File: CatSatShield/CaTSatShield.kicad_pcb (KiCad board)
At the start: 2 copper layers, 67.6 x 25 mm, 18 parts, among them J1 , J2 , J3 BME280, J4 CCS811

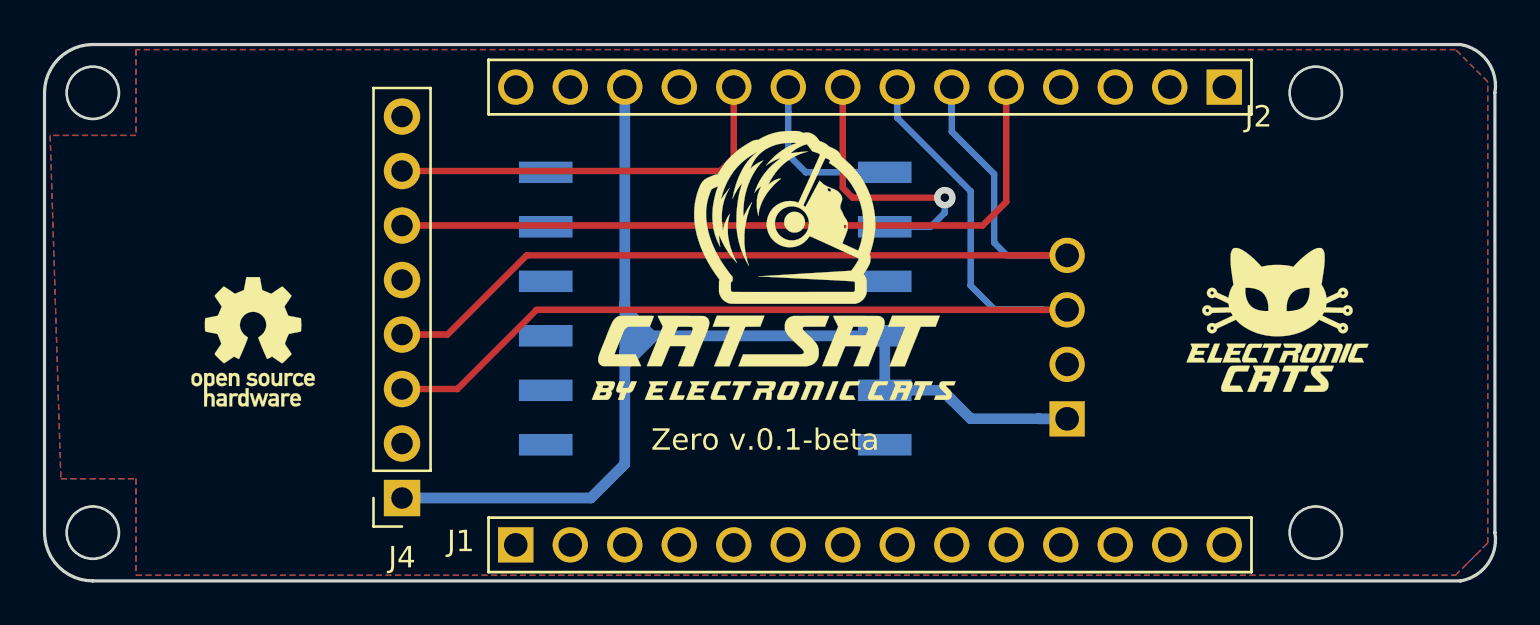
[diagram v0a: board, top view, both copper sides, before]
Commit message: connected pin wakeA6
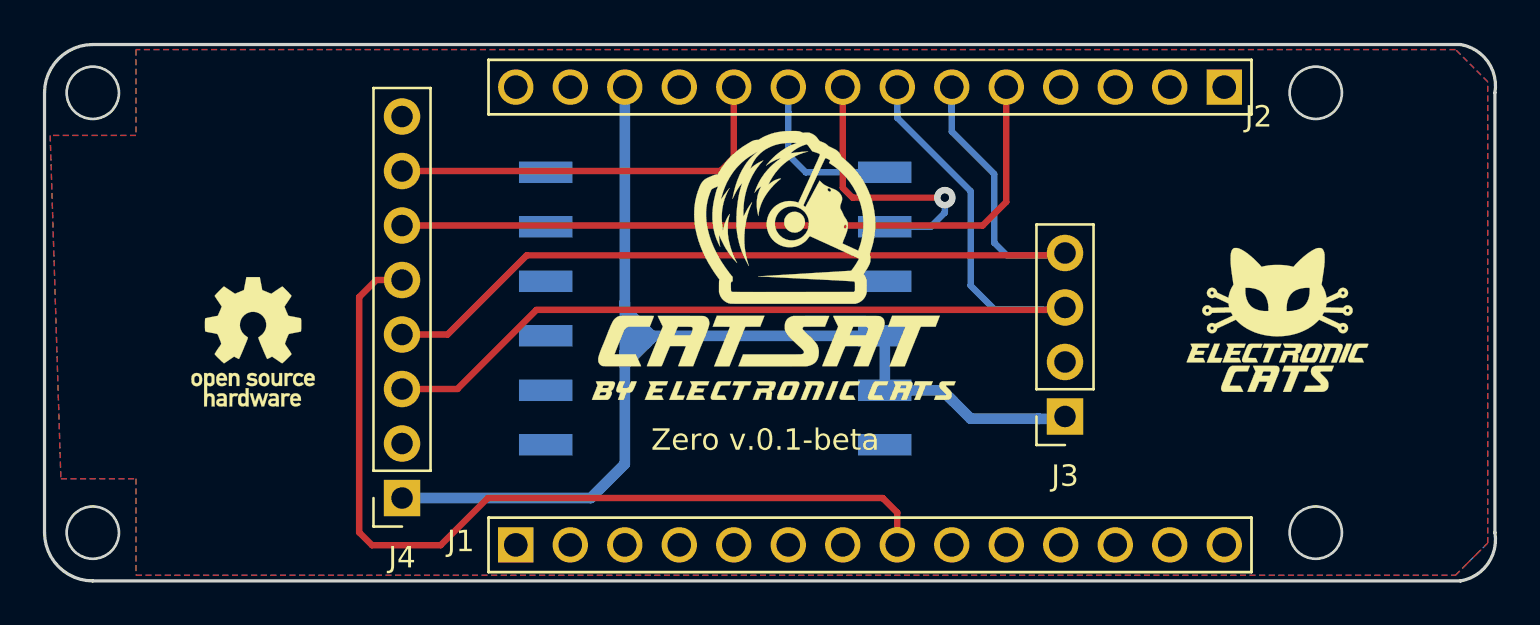
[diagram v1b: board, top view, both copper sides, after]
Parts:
- J3: footprint Pines:61300411121 -> Connector_PinSocket_2.54mm:PinSocket_1x04_P2.54mm_Vertical; moved to F.Cu
- moved J3 3.70 mm to (161.8, 106.1), turned to 180 degrees
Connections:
- J1 pad 8: /WAKE-A6 -> /WAKEA6
- J4 pad 5: /WAK-A6 -> /WAKEA6
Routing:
- net /WAKEA6: track 0.00 -> 41.3 mm

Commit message: update to version 0.3
Update silks
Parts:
- G***: moved to B.Cu
- moved G*** 48.0 mm to (123.8, 102.4), turned to 180 degrees
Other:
- board text added: "Zero v.0.3"
- board text removed: "Zero v.0.1-beta"

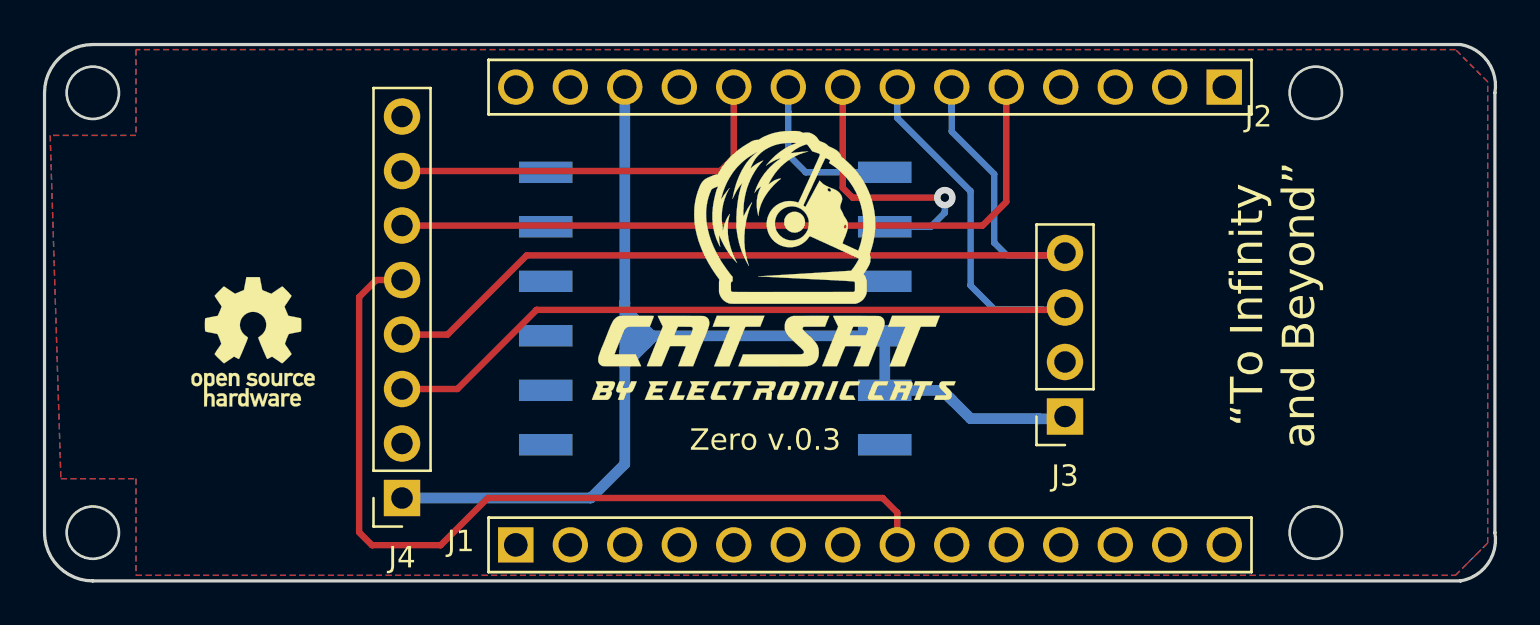
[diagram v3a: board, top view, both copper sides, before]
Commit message: track width
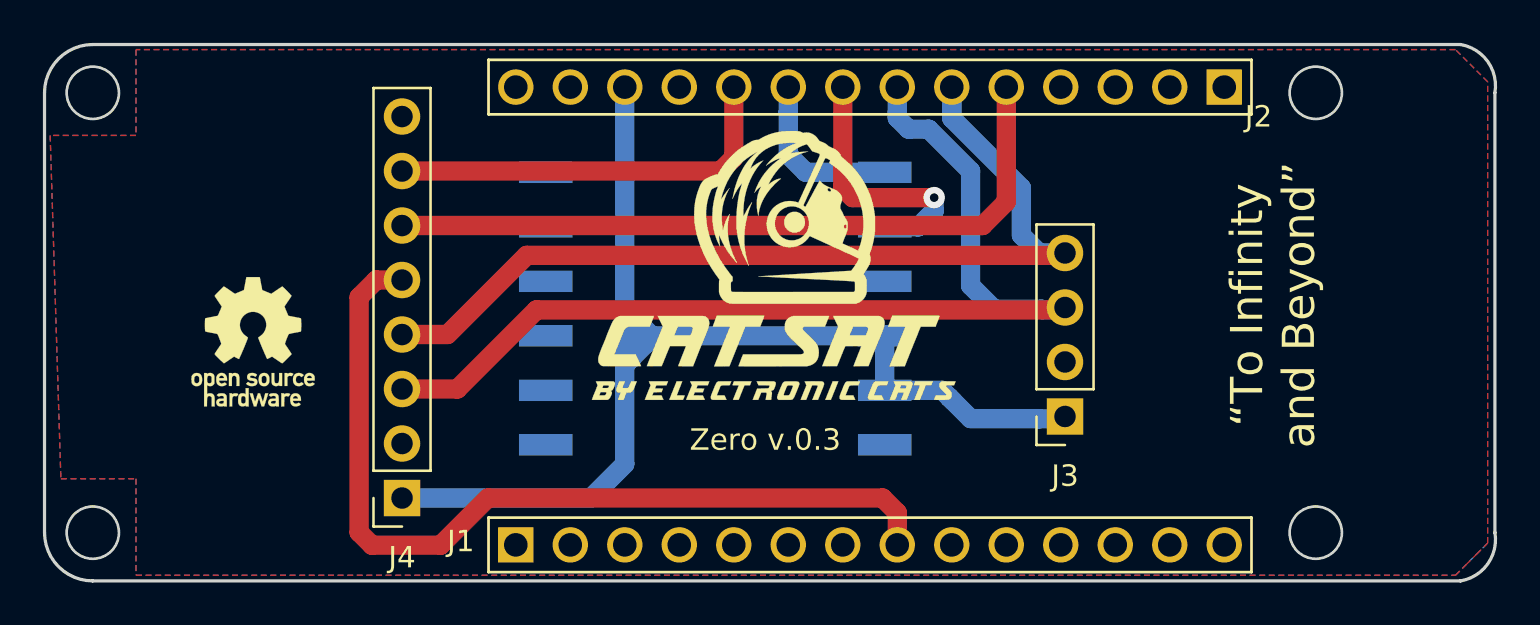
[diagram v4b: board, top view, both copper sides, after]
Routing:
- net /SDA: track 45.4 -> 44.3 mm
- net /RX: track 13.4 -> 12.4 mm
- net /SCL: track 48.2 -> 48.7 mm
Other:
- net class Default: trace_width 0.3 -> 0.9
- net class SOURCE: trace_width 0.5 -> 0.9

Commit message: pin name
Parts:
- moved G*** 2.90 mm to (147.8, 101.9), turned to 180 degrees
- turned REF*** to 180 degrees
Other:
- board text added: "1"
- board text added: "ADO"
- board text added: "GND"
- board text added: "RST"
- board text added: "SCL"
- board text added: "SDA"
- board text added: "UNICCS"
- board text added: "VCC"
- board text added: "WAKE"
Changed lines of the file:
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@@
   (general
     (thickness 1.6)
-    (drawings 55)
+    (drawings 68)
     (tracks 80)
     (zones 0)
@@
   )
   (module Aesthetics:catsat (layer Top)
-    (at 148.59 99.06)
-    (fp_text reference G*** (at 0 0) (layer F.SilkS) hide
+    (at 147.828 101.854 180)
+    (fp_text reference G*** (at 0 0 180) (layer F.SilkS) hide
       (effects (font (size 1.524 1.524) (thickness 0.3)))
     )
-    (fp_text value LOGO (at 0.75 0) (layer F.SilkS) hide
+    (fp_text value LOGO (at 0.75 0 180) (layer F.SilkS) hide
       (effects (font (size 1.524 1.524) (thickness 0.3)))
     )
@@
   )
   (module Symbols:OSHW-Logo_5.7x6mm_SilkScreen (layer Top)
-    (at 123.952 102.616)
+    (at 123.952 102.616 180)
     (descr "Open Source Hardware Logo")
     (tags "Logo OSHW")
     (attr virtual)
-    (fp_text reference REF*** (at 0 0) (layer F.SilkS) hide
+    (fp_text reference REF*** (at 0 0 180) (layer F.SilkS) hide
       (effects (font (size 1 1) (thickness 0.15)))
     )
-    (fp_text value OSHW-Logo_5.7x6mm_SilkScreen (at 0.75 0) (layer F.Fab) hide
+    (fp_text value OSHW-Logo_5.7x6mm_SilkScreen (at 0.75 0 180) (layer F.Fab) hide
       (effects (font (size 1 1) (thickness 0.15)))
     )
@@
     (descr "Through hole straight socket strip, 1x08, 2.54mm pitch, single row (from Kicad 4.0.7), script generated")
     (tags "Through hole socket strip THT 1x08 2.54mm single row")
-    (fp_text reference J4 (at 0 -2.77 180) (layer F.SilkS)
+    (fp_text reference J4 (at 0 -2.77) (layer F.SilkS)
       (effects (font (size 1 1) (thickness 0.15)))
     )
@@
     (descr "Through hole straight socket strip, 1x04, 2.54mm pitch, single row (from Kicad 4.0.7), script generated")
     (tags "Through hole socket strip THT 1x04 2.54mm single row")
-    (fp_text reference J3 (at 0 -2.77 180) (layer F.SilkS)
+    (fp_text reference J3 (at 0 -2.77) (layer F.SilkS)
       (effects (font (size 1 1) (thickness 0.15)))
     )
@@
     )
   )
+  (gr_text ADO (at 134.112 92.456 180) (layer F.SilkS)
+    (effects (font (size 1 1) (thickness 0.25)))
+  )
+  (gr_text RST (at 134.112 94.996 180) (layer F.SilkS)
+    (effects (font (size 1 1) (thickness 0.25)))
+  )
+  (gr_text UNICCS (at 135.382 97.536 180) (layer F.SilkS)
+    (effects (font (size 1 1) (thickness 0.25)))
+  )
+  (gr_text WAKE (at 134.62 100.076 180) (layer F.SilkS)
+    (effects (font (size 1 1) (thickness 0.25)))
+  )
+  (gr_text SDA (at 134.112 102.616 180) (layer F.SilkS)
+    (effects (font (size 1 1) (thickness 0.25)))
+  )
+  (gr_text SCL (at 134.112 105.156 180) (layer F.SilkS)
+    (effects (font (size 1 1) (thickness 0.25)))
+  )
+  (gr_text SDA (at 165.1 98.552 180) (layer F.SilkS)
+    (effects (font (size 1 1) (thickness 0.25)))
+  )
+  (gr_text SCL (at 165.1 101.092 180) (layer F.SilkS)
+    (effects (font (size 1 1) (thickness 0.25)))
+  )
+  (gr_text GND (at 165.1 103.632 180) (layer F.SilkS)
+    (effects (font (size 1 1) (thickness 0.25)))
+  )
+  (gr_text GND (at 134.112 107.696 180) (layer F.SilkS)
+    (effects (font (size 1 1) (thickness 0.25)))
+  )
+  (gr_text VCC (at 165.1 106.172 180) (layer F.SilkS)
+    (effects (font (size 1 1) (thickness 0.25)))
+  )
+  (gr_text VCC (at 134.366 109.982 180) (layer F.SilkS)
+    (effects (font (size 1 1) (thickness 0.25)))
+  )
+  (gr_text 1 (at 155.702 94.234) (layer B.SilkS)
+    (effects (font (size 1.5 1.5) (thickness 0.3)) (justify mirror))
+  )
   (dimension 67.550074 (width 0.3) (layer Margin)
     (gr_text "67,550 mm" (at 148.033329 69.748974 -0.08481974487) (layer Margin)
@@
     (arrow2b (pts (xy 181.88262 104.892539) (xy 180.750137 105.467327)))
   )
-  (gr_text "Zero v.0.3" (at 147.828 107.188) (layer F.SilkS)
+  (gr_text "Zero v.0.3" (at 148.336 94.234 180) (layer F.SilkS)
     (effects (font (size 1 1) (thickness 0.25)))
   )
